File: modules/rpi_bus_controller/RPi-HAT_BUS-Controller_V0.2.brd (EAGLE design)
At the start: 65 x 56 mm, 52 parts, among them IC1 MC34063AD, IC2 ADUM1201ARZ, IC3 P89LPC922FDH,512FDH, IC4 24LC-I/OT, Q1 ASF1, T1 BC856, T2 BCP52, T3 BC847

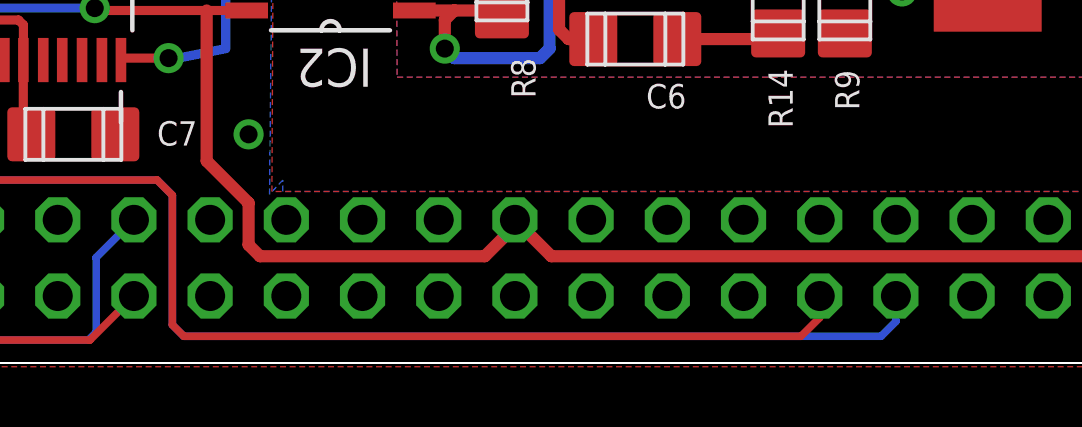
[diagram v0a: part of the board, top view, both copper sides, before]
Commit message: TXD RXD getauscht
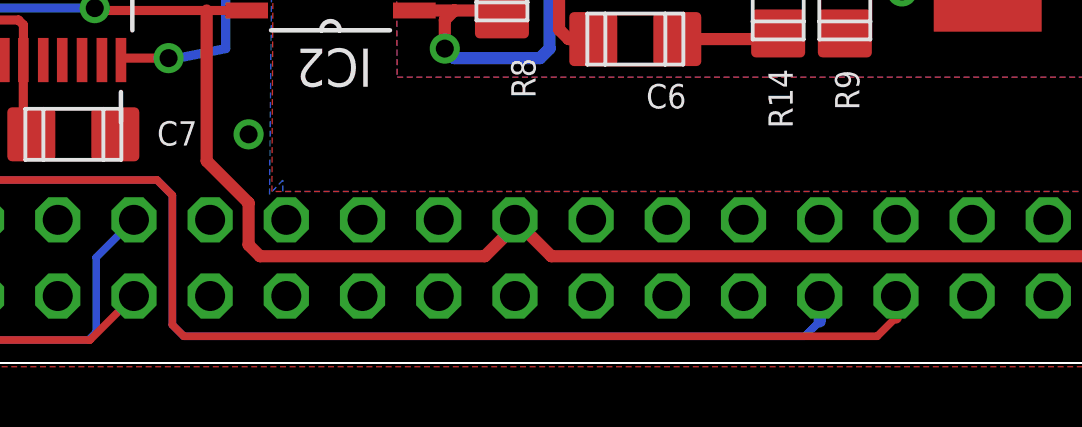
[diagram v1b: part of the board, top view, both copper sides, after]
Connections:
- net RXD: now also JP2.8; no longer JP2.10
- net TXD: now also JP2.10; no longer JP2.8
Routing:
- net TXD: track 59.1 -> 56.5 mm
- net RXD: track 45.8 -> 48.3 mm
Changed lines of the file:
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@@
 </signal>
 <signal name="TXD">
-<contactref element="JP2" pad="8"/>
 <contactref element="JP1" pad="4"/>
 <contactref element="IC3" pad="12"/>
-<wire x1="49.01" y1="2.23" x2="49.01" y2="1.385" width="0.254" layer="16"/>
-<wire x1="49.01" y1="1.385" x2="48.514" y2="0.889" width="0.254" layer="16"/>
-<wire x1="48.514" y1="0.889" x2="25.273" y2="0.889" width="0.254" layer="16"/>
+<wire x1="46.47" y1="1.385" x2="45.974" y2="0.889" width="0.254" layer="16"/>
+<wire x1="45.974" y1="0.889" x2="25.273" y2="0.889" width="0.254" layer="16"/>
 <wire x1="25.273" y1="0.889" x2="24.892" y2="1.27" width="0.254" layer="16"/>
 <wire x1="24.892" y1="1.27" x2="24.892" y2="5.588" width="0.254" layer="16"/>
@@
 <wire x1="17.9705" y1="11.2395" x2="16.51" y2="12.7" width="0.4064" layer="1"/>
 <wire x1="16.51" y1="12.7" x2="12.7" y2="12.7" width="0.4064" layer="1"/>
+<contactref element="JP2" pad="10"/>
+<wire x1="46.47" y1="2.23" x2="46.47" y2="1.385" width="0.4064" layer="16"/>
 </signal>
 <signal name="RXD">
-<contactref element="JP2" pad="10"/>
 <contactref element="JP1" pad="5"/>
 <contactref element="IC3" pad="11"/>
-<wire x1="46.47" y1="2.23" x2="46.47" y2="1.512" width="0.254" layer="1"/>
-<wire x1="46.47" y1="1.512" x2="45.847" y2="0.889" width="0.254" layer="1"/>
-<wire x1="45.847" y1="0.889" x2="25.273" y2="0.889" width="0.254" layer="1"/>
+<wire x1="49.01" y1="1.512" x2="48.387" y2="0.889" width="0.254" layer="1"/>
+<wire x1="48.387" y1="0.889" x2="25.273" y2="0.889" width="0.254" layer="1"/>
 <wire x1="25.273" y1="0.889" x2="24.892" y2="1.27" width="0.254" layer="1"/>
 <wire x1="24.892" y1="1.27" x2="24.892" y2="5.588" width="0.254" layer="1"/>
@@
 <wire x1="17.3355" y1="10.0965" x2="14.716125" y2="10.0965" width="0.3048" layer="1"/>
 <wire x1="14.716125" y1="10.0965" x2="14.732" y2="10.080625" width="0.4064" layer="1"/>
+<contactref element="JP2" pad="8"/>
+<wire x1="49.01" y1="1.512" x2="49.01" y2="2.23" width="0.4064" layer="1"/>
 </signal>
 <signal name="ID_SC">
